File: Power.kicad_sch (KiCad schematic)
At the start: 55 parts, among them J11 Conn_01x02_Socket, Q3 2N2222, U21 MIC23201YML-TR, U29 AP7361C-33E, U30 MP8795

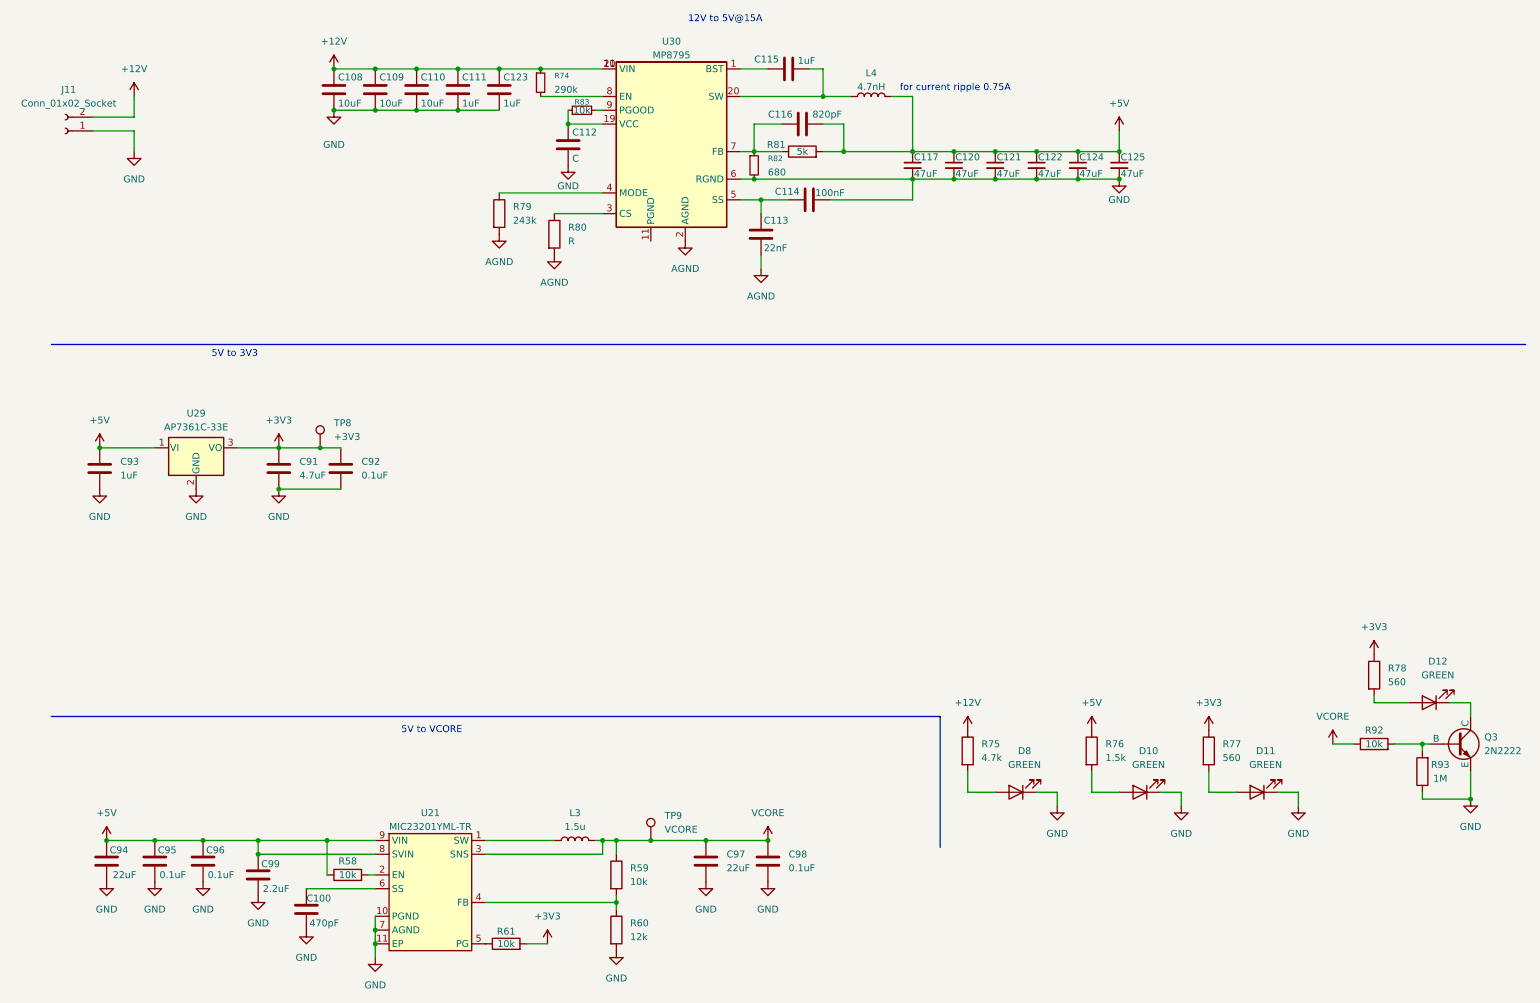
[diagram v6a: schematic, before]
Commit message: eFuse added
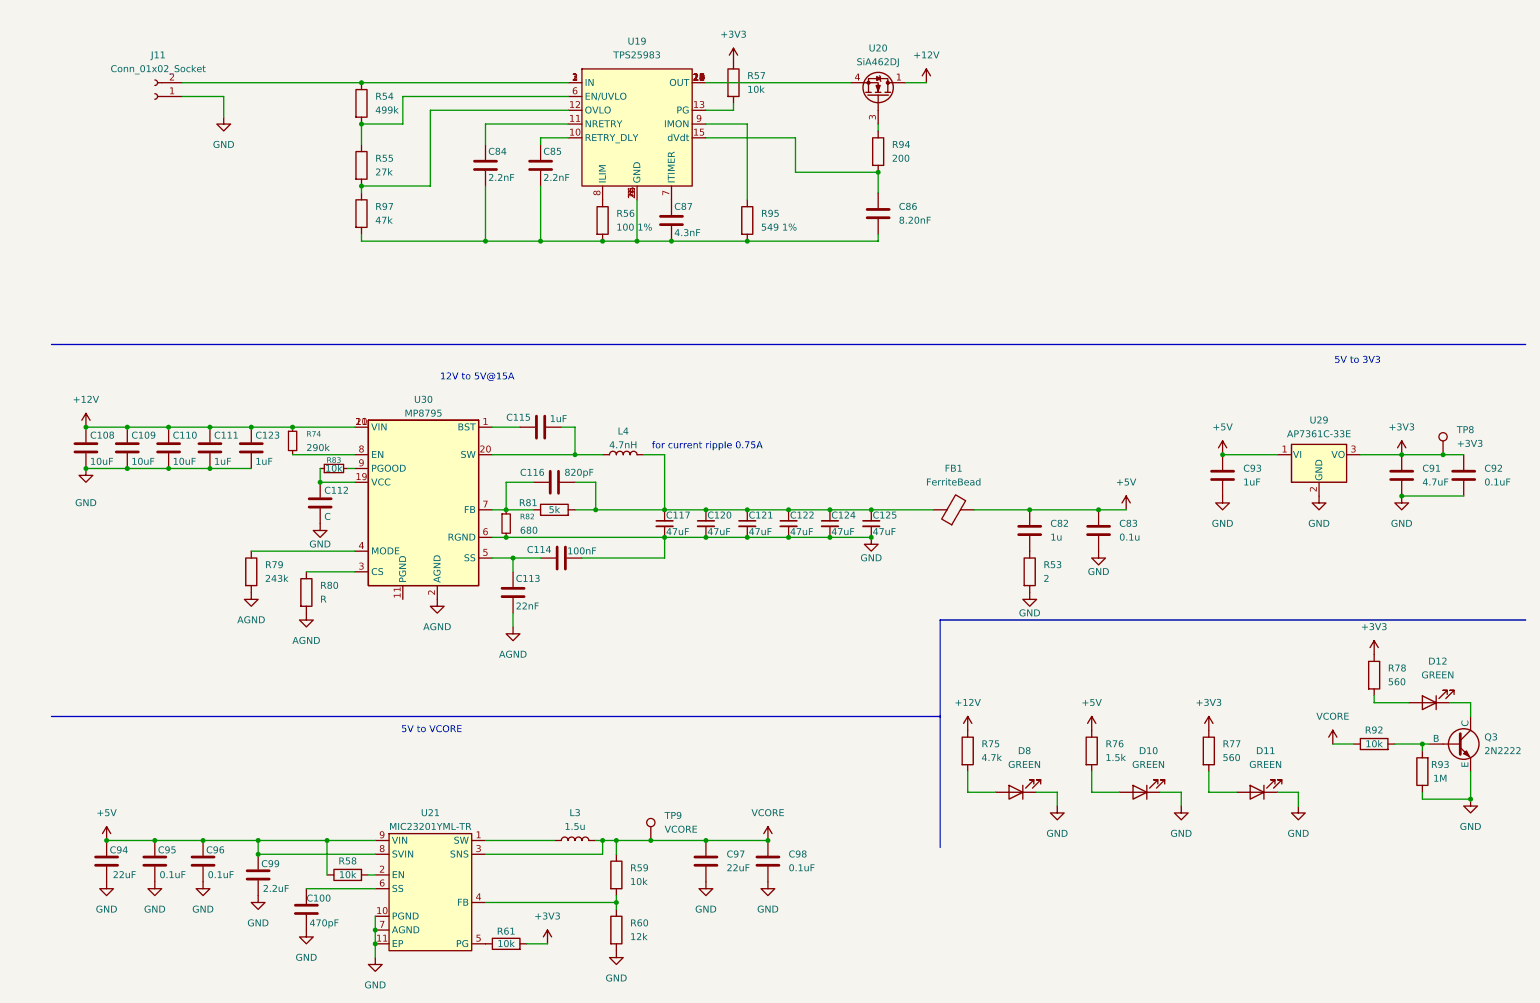
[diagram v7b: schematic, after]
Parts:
- added C82: 1u, symbol Device:C
- added C83: 0.1u, symbol Device:C
- added C84, C85: 2.2nF, symbol Device:C
- added C86: 8.20nF, symbol Device:C
- added C87: 4.3nF, symbol Device:C
- added FB1: FerriteBead, symbol Device:FerriteBead
- added R53: 2, symbol Device:R
- added R54: 499k, symbol Device:R
- added R55: 27k, symbol Device:R
- added R56: 100 1%, symbol Device:R
- added R57: 10k, symbol Device:R
- added R94: 200, symbol Device:R
- added R95: 549 1%, symbol Device:R
- added R97: 47k, symbol Device:R
- added U19: TPS25983, symbol Snapeda:TPS25983
- added U20: SiA462DJ, Package_TO_SOT_SMD:Vishay_PowerPAK_SC70-6L_Single, symbol Transistor_FET:SiA462DJ
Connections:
- net +12V: now also U20.1 (D); no longer J11.2 (Pin_2)
- net +3V3: now also R57.1
- net +5V: now also C82.1, C83.1, FB1.2; no longer C116.2, C117.1, C120.1, C121.1, C122.1, C124.1, C125.1, L4.2, R81.2
- net GND: now also C83.2, R53.2
- new net: C116.2, C117.1, C120.1, C121.1, C122.1, C124.1, C125.1, FB1.1, L4.2, R81.2
- new net: J11.2 (Pin_2), R54.1, U19.1 (IN), U19.2 (IN), U19.3 (IN)
- new net: R54.2, R55.1, U19.6 (EN/UVLO)
- new net: R95.1, U19.9 (IMON)
- new net: C84.2, C85.2, C86.2, C87.2, R56.2, R95.2, R97.2, U19.14 (GND), U19.26 (GND), U19.4 (GND), U19.5 (GND)
- new net: C87.1, U19.7 (ITIMER)
- new net: C85.1, U19.10 (RETRY_DLY)
- new net: C84.1, U19.11 (NRETRY)
- new net: R55.2, R97.1, U19.12 (OVLO)
- new net: R57.2, U19.13 (PG)
- new net: C86.1, R94.2, U19.15 (dVdt)
- new net: U19.17 (OUT), U19.18 (OUT), U19.19 (OUT), U19.20 (OUT), U19.21 (OUT), U19.22 (OUT), U19.23 (OUT), U19.24 (OUT), U19.25 (OUT), U20.4 (S)
- new net: R56.1, U19.8 (ILIM)
- new net: C82.2, R53.1
- new net: R94.1, U20.3 (G)
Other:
- moved on the sheet: C108, C109, C110, C111, C112, C113, C114, C115, C116, C117, C120, C121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

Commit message: Ferrite Breads added for 5V, TVS and ESD diodes added
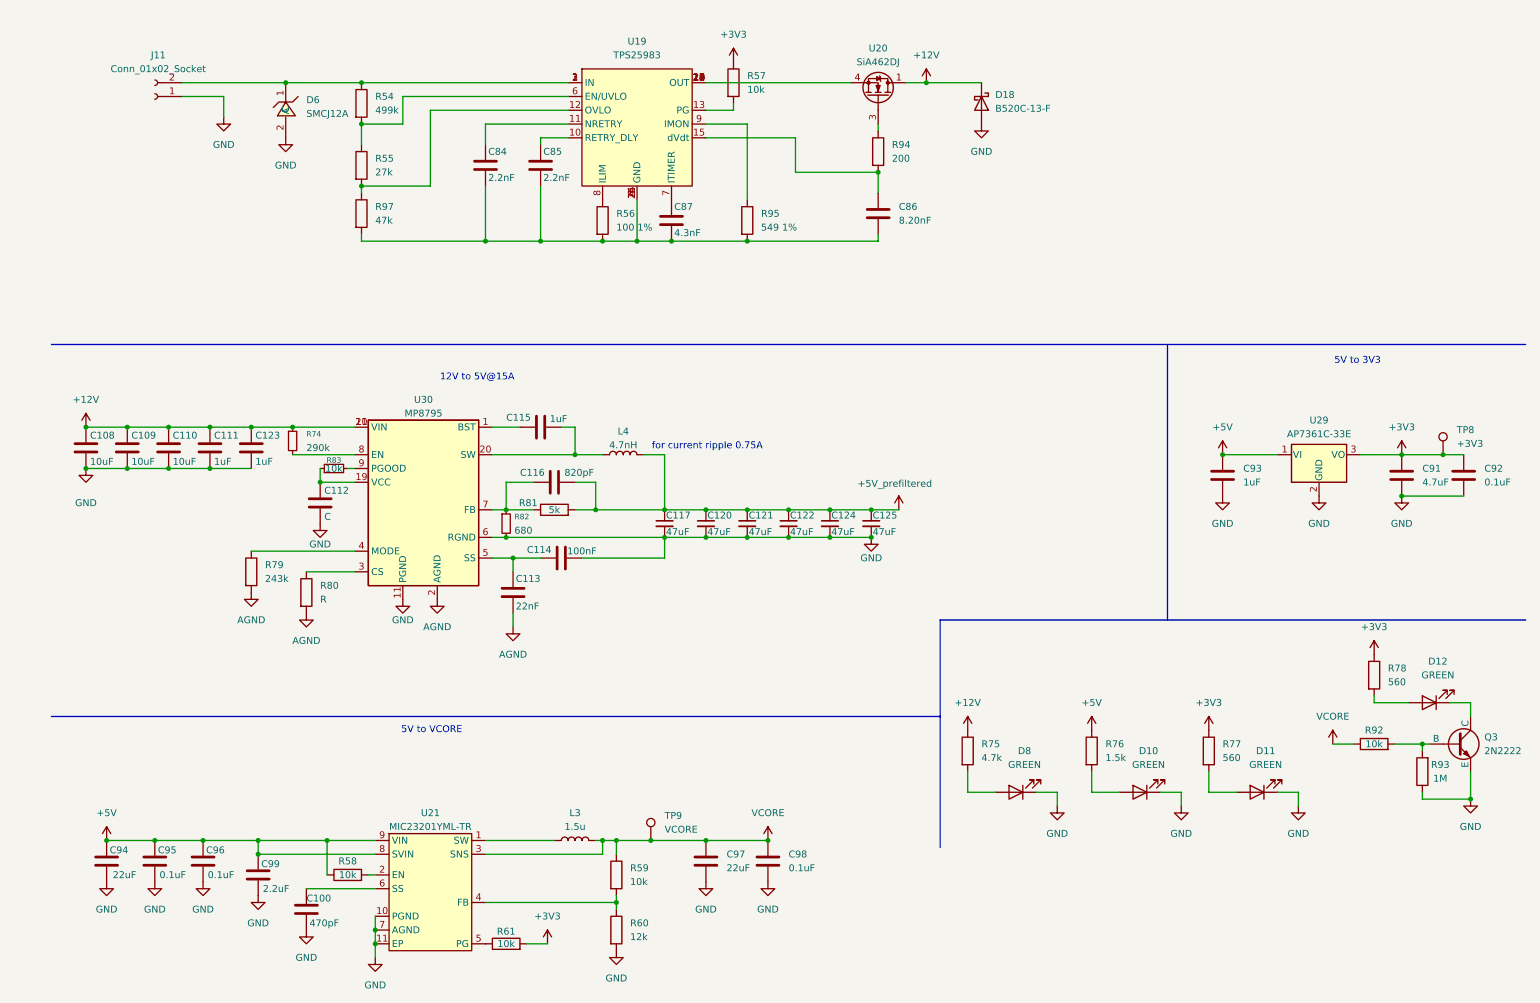
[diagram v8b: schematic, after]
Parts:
- removed C82: 1u, symbol Device:C
- removed C83: 0.1u, symbol Device:C
- removed FB1: FerriteBead, symbol Device:FerriteBead
- removed R53: 2, symbol Device:R
- added D18: B520C-13-F, symbol Device:D_Schottky
- added D6: SMCJ12A, EasyEDA:X2SON-2_L0.6-W0.3-P0.35, symbol EasyEDA:ESD441DPLR
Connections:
- net +12V: now also D18.1 (K)
- net GND: now also U30.11 (PGND), D18.2 (A), D6.2 (A)
- net +5V_prefiltered: now reaches C116.2, C117.1, C120.1, C121.1, C122.1, C124.1, C125.1, L4.2, R81.2
- net at J11.2 (Pin_2), R54.1, U19.1 (IN)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: now also D6.1 (C)
